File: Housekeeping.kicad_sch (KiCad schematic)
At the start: 78 parts, among them J8 IRIG IN, U123 MAX4896, U15 AT24C64D-SSHM, U19 74AVC4T245, U3701 SI5330B-B00206-GM, U38 SN74LVC1T45DBV

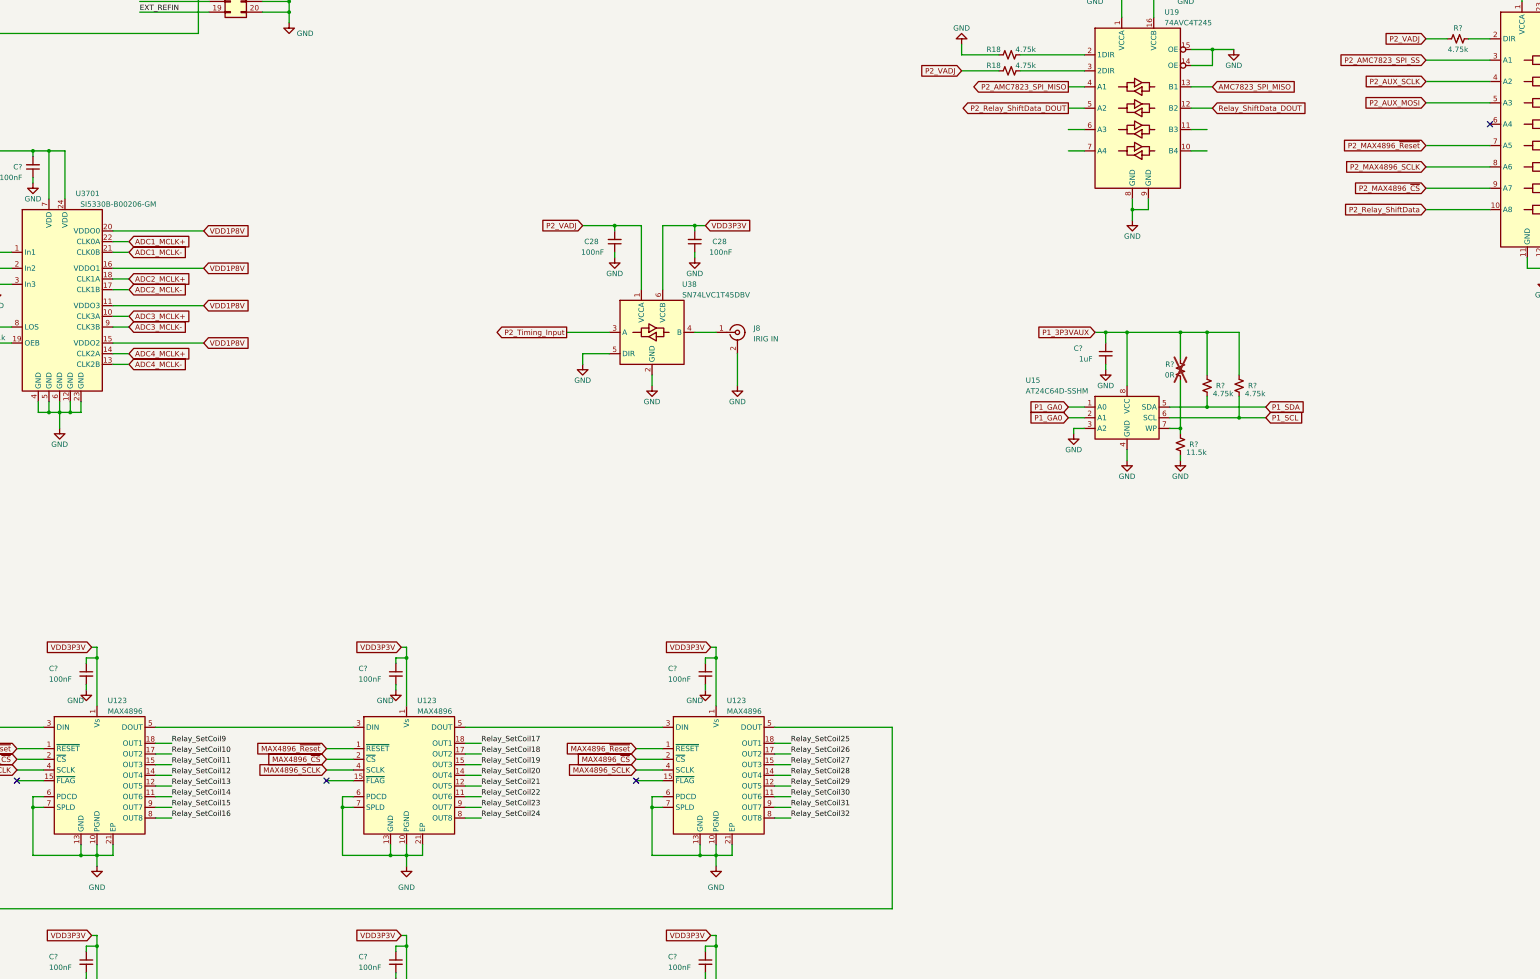
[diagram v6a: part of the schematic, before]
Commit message: Schematic Updates
Updated:
-Fixed AMC7823 labels
-Added present detect signals on FMC
-Added ferrite beads in Power Section and AFE
-Added 0R in power section
-Revised EEPROM connections
-Changed +5V SMPS part to one with an integrated inductor
-Added more detail on FMC connector
-Added file showing SMPS calculations
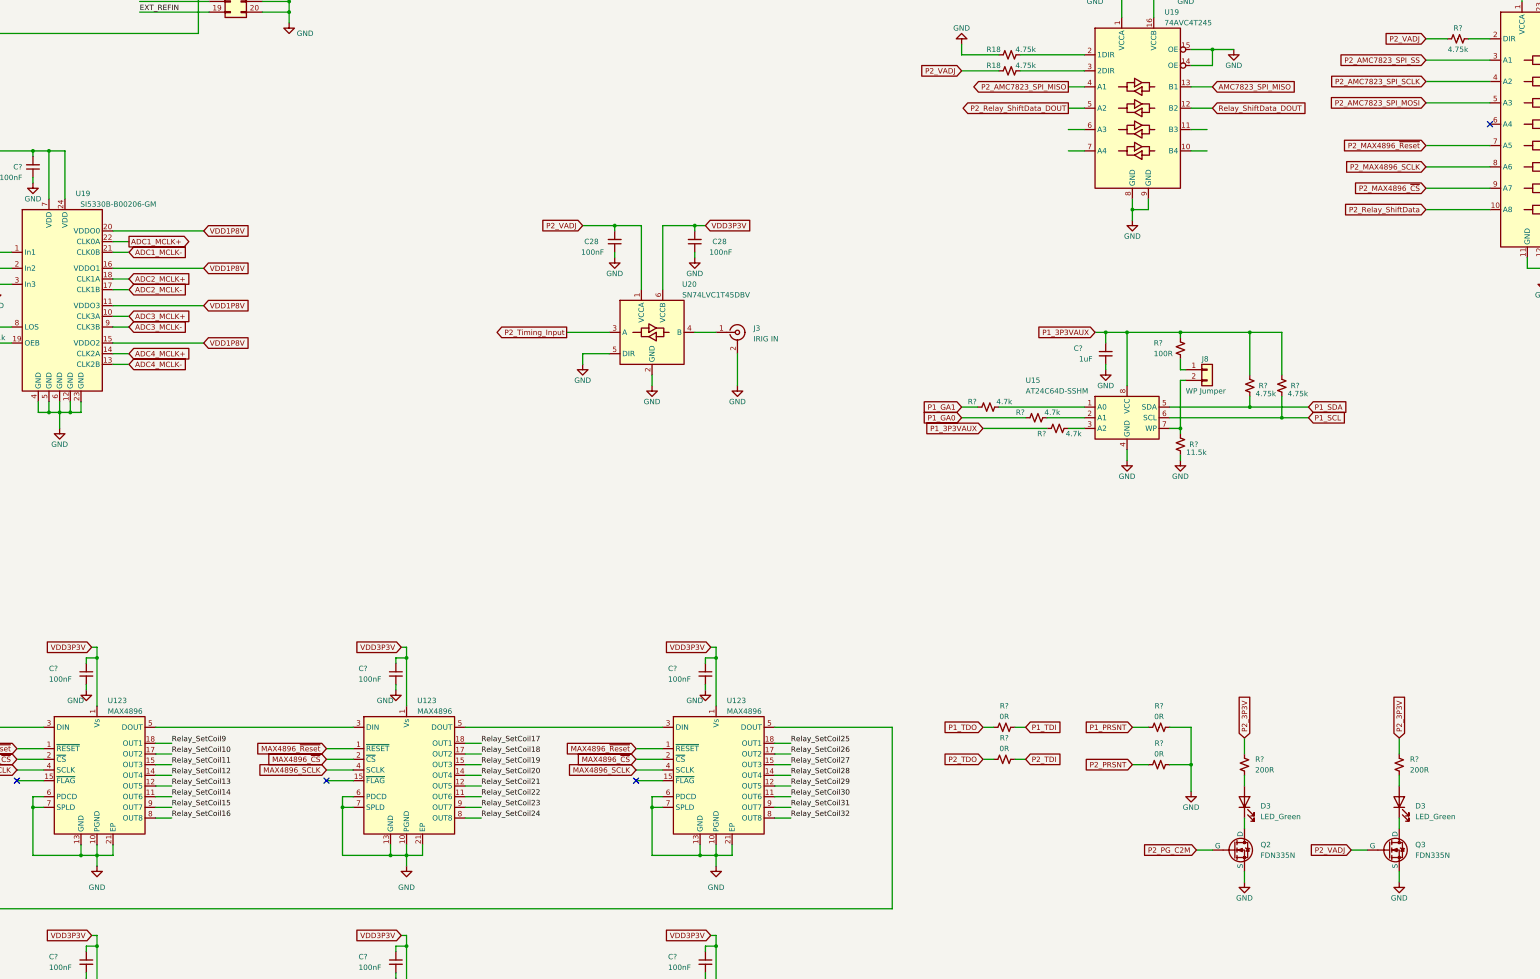
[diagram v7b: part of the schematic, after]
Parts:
- removed R?: 0R, symbol Device:R_Small_US
- added D3 (x2): LED_Green, symbol Device:LED
- added J8: WP Jumper, symbol Connector_Generic:Conn_01x02
- added Q2, Q3: FDN335N, symbol Simulation_SPICE:NMOS
- added R? (x4): 0R, Capacitor_SMD:C_0603_1608Metric, symbol Device:R_Small_US
- added R? (x3): 4.7k, symbol Device:R_Small_US
- added R?: 100R, symbol Device:R_Small_US
- added R? (x2): 200R, Capacitor_SMD:C_0603_1608Metric, symbol Device:R_Small_US
- renumbered J8 to J3, U3701 to U19, U38 to U20
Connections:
- net GND: now also Q2.3 (S), Q3.3 (S), R?.2, R?.2; no longer U15.3 (A2)
- net P1_3P3VAUX: now also R?.1, R?.1
- net P1_GA0: now also R?.1; no longer U15.1 (A0), U15.2 (A1)
- net P2_VADJ: now also Q3.2 (G)
- net at R?.1, U15.7 (WP): now also J8.2 (Pin_2)
- net P2_AUX_MOSI renamed P2_AMC7823_SPI_MOSI
- net P2_AUX_SCLK renamed P2_AMC7823_SPI_SCLK
- new net: J8.1 (Pin_1), R?.2
- new net: R?.2, U15.1 (A0)
- new net: D3.1 (K), Q2.1 (D)
- new net: D3.2 (A), R?.1 (x2)
- new net: R?.2, U15.3 (A2)
- new net: D3.1 (K), Q3.1 (D)
- new net: R?.2, U15.2 (A1)
- new net P1_GA1: R?.1
- new net P1_PRSNT: R?.1
- new net P1_TDI: R?.2
- new net P1_TDO: R?.1
- new net P2_3P3V: R?.2, R?.2
- new net P2_PG_C2M: Q2.2 (G)
- new net P2_PRSNT: R?.1
- new net P2_TDI: R?.2
- new net P2_TDO: R?.1
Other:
- moved on the sheet: R?

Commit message: Updated Schematic
-Changed PPS input signal buffer
-Made Tweaks to Power Supply section  (Many involving the LT3097) as suggested by Trent.
- general schematic clean up for readability
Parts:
- removed C? (x7): 150pF, symbol Device:C_Small
- removed C? (x6): 100nF, symbol Device:C_Small
- removed R?: 11.5k, symbol Device:R_Small_US
- removed R? (x4): 22k, symbol Device:R_Small_US
- removed R?: 100R, symbol Device:R_Small_US
- removed R? (x2): 4.7k, symbol Device:R_Small_US
- removed U20: SN74LVC1T45DBV, Package_TO_SOT_SMD:SOT-23-6, symbol Logic_LevelTranslator:SN74LVC1T45DBV
- added C? (x6): 100nF, Capacitor_SMD:C_0603_1608Metric, symbol Device:C_Small
- added C? (x5): 150pF, Capacitor_SMD:C_0603_1608Metric, symbol Device:C_Small
- added R? (x2): 38.3k, Resistor_SMD:R_0603_1608Metric, symbol Device:R_Small_US
- added R?: 11.5k, symbol Device:R_Small_US
- added R? (x2): 4.75k, Resistor_SMD:R_0603_1608Metric, symbol Device:R_Small_US
- added R? (x2): 100k, Resistor_SMD:R_0603_1608Metric, symbol Device:R_Small_US
- added R? (x4): 22k, Resistor_SMD:R_0603_1608Metric, symbol Device:R_Small_US
- added R? (x2): 4.75k, symbol Device:R_Small_US
- added U36: TL071H, symbol Amplifier_Operational:TL071
- added U37: TXU0101, Package_TO_SOT_SMD:SOT-23-6, symbol Logic_LevelTranslator:SN74AUP1T34DCK
- C?: footprint (none) -> Capacitor_SMD:C_0603_1608Metric; MPN (none) -> GRM1885C1H151JA01D; Note X5R 25V 1206 -> (none)
- D?: footprint (none) -> LED_SMD:LED_0603_1608Metric; MPN (none) -> LTST-C190GKT
- J5: renamed from J3; value IRIG IN -> PPS IN
- R? (x6): footprint (none) -> Resistor_SMD:R_0603_1608Metric; MPN (none) -> RC0603FR-074K75L
- R?: value 4.7k -> 4.75k
- R? (x2): footprint (none) -> Resistor_SMD:R_0603_1608Metric; MPN (none) -> RC0603FR-0722KL
- R?: MPN (none) -> RC0603FR-07150RL
- U?: MP AMC7823IRTAR -> (none); MPN (none) -> AMC7823IRTAR
- renumbered J8 to J6, Q2 to Q1, Q3 to Q2, U19 to U16
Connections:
- net AD0: now also J?.3 (Pin_3), C?.2; no longer J?.7 (Pin_7)
- net AD1: now also J?.1 (Pin_1), C?.2; no longer J?.5 (Pin_5)
- net AD2: now also R?.2, U36.1; no longer J?.3 (Pin_3)
- net AD3: now also R?.1, R?.2; no longer J?.1 (Pin_1)
- net DAC5: now also J?.7 (Pin_7)
- net DAC6: now also J?.5 (Pin_5)
- net GND: now also J6.2 (Pin_2), C?.1, C?.1, C?.1, C?.1, C?.1, C?.2, C?.2, C?.2, C?.2, C?.2, C?.2, R?.2, R?.2, U36.3 (+), U37.2 (GND)
- net GPIO0: now also R?.2
- net GPIO1: now also R?.2
- net GPIO2: now also R?.2
- net GPIO3: now also R?.2
- net P1_3P3VAUX: now also R?.1, R?.1
- net P1_GA0: now also R?.1
- net P2_Timing_Input: now also U37.4 (B)
- net P2_VADJ: now also C?.1, C?.1, C?.1, U37.6 (VCCB)
- net VDD1P8V: now also C?.1, C?.1, C?.1
- net VDD3P3V: now also C?.2, C?.2, C?.2, R?.1, R?.1, R?.1, R?.1; no longer C28.2
- net at U15.7 (WP): now also J6.1 (Pin_1), R?.2; no longer J6.2 (Pin_2)
- net at J5.1 (In): now also U37.3 (A)
- net at U15.3 (A2): now also R?.2
- net at U15.2 (A1): now also R?.2
- new net: R?.1, R?.1, R?.2
- new net: R?.1, R?.2, U36.4 (-)
- new net +5V: C28.2, U37.1 (VCCA), U37.5 (OE)
- new net 15V+: R?.1, U36.5 (V+)
- new net 15V-: R?.1, U36.2 (V-)
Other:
- note added: "Board Present"
- note added: "EEPROM"
- note added: "LVDS Clock Splitter"
- note added: "Level Shifters"
- note added: "Managment DAQ"
- note added: "Relay Drivers"
- moved on the sheet: C28, C?, D3, D?, J5, J6, J?, Q1, Q2, R18, R?, U123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
